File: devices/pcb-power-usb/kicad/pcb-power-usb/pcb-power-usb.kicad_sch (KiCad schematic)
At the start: 56 parts, among them J1 USB_A, J10 Conn_01x01, J2 USB_A, J3 USB_A, J4 USB_A, J5 USB_A, J6 USB_A, J7 USB_A, J8 USB_A, J9 Conn_01x01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

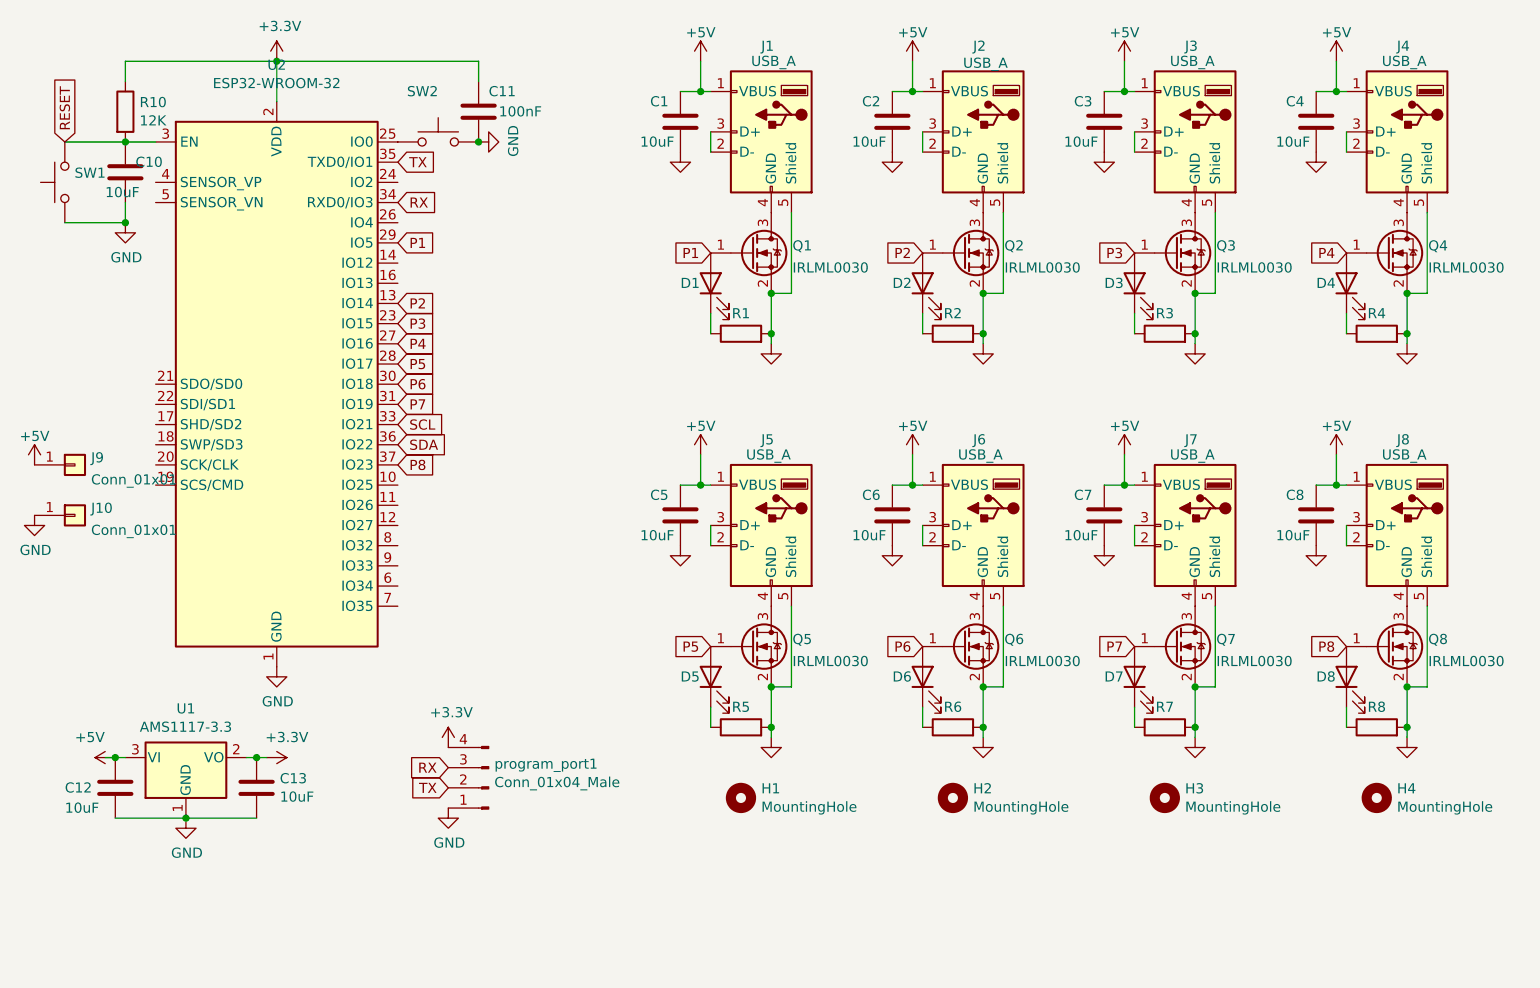
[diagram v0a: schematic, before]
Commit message: complete readme with pictures
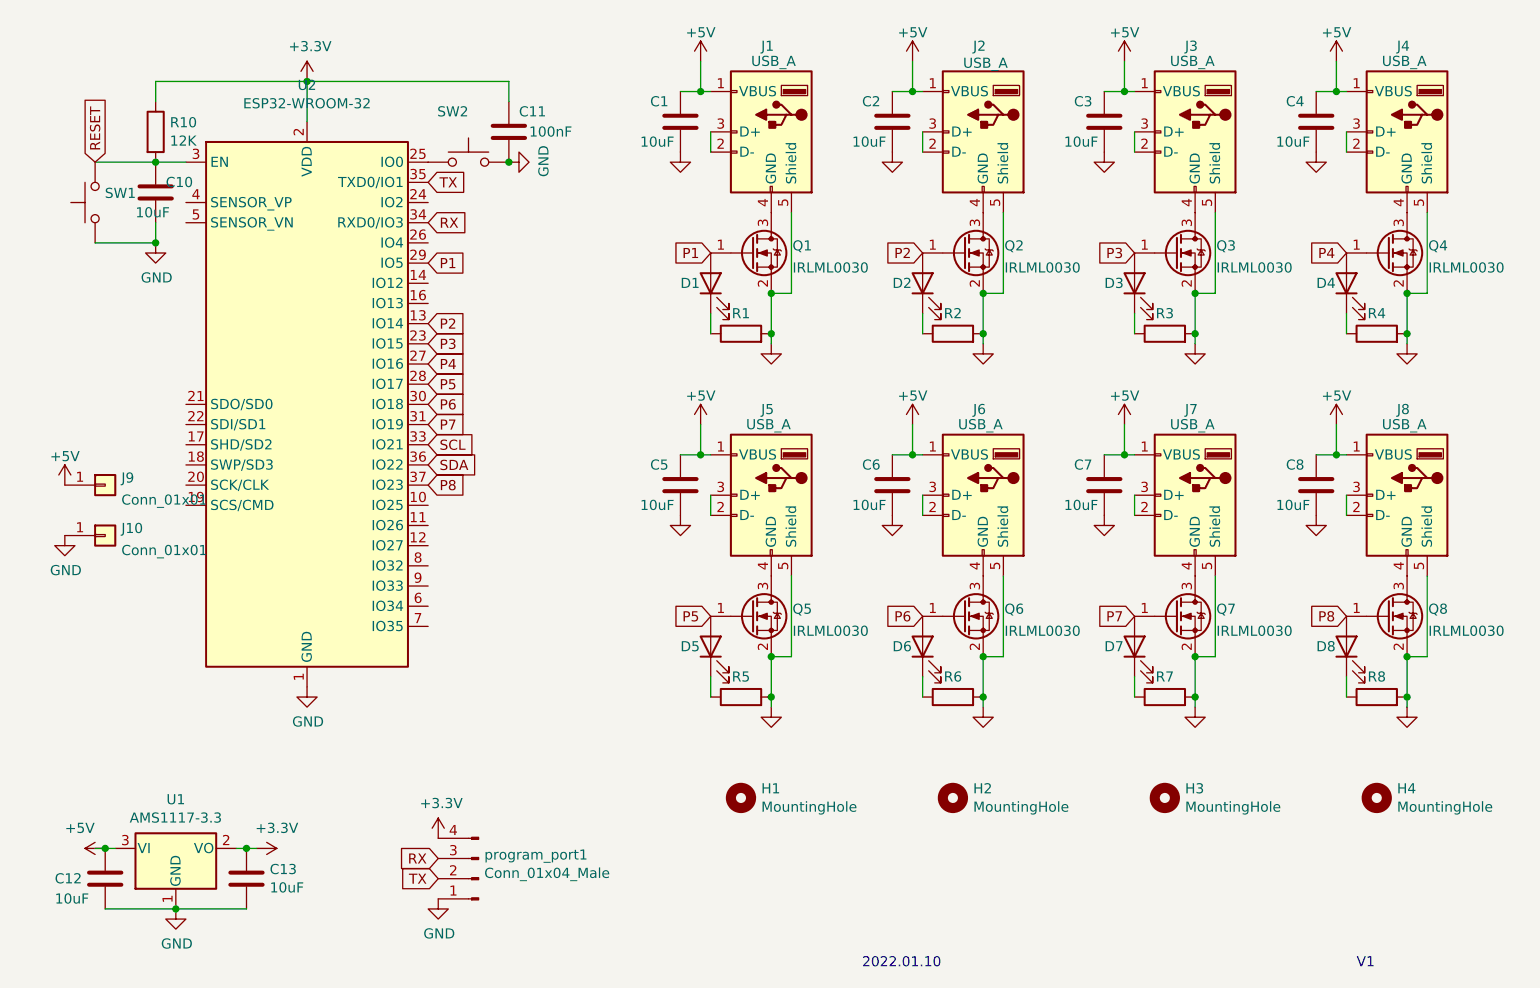
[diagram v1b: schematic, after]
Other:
- note added: "2022.01.10"
- note added: "V1"
- moved on the sheet: C10, C11, C12, C13, C5, C6, C7, C8, D5, D6, D7, D8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
